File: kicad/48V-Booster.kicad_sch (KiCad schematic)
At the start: 14 parts, among them J9 48V out, U3 LM317_TO-220

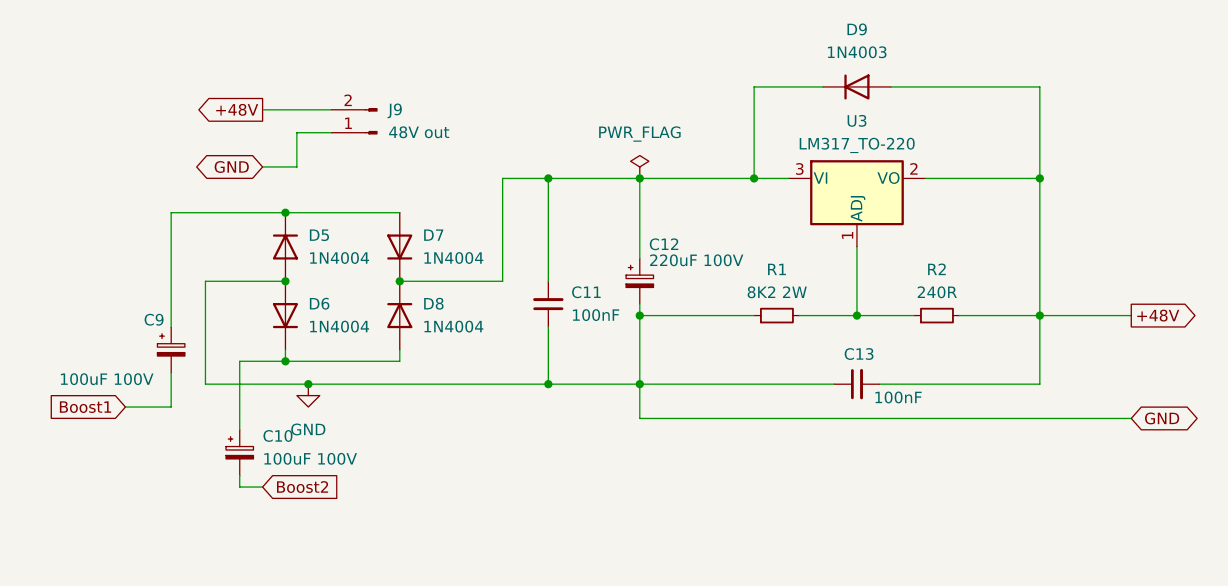
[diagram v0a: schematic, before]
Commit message: Board done - needs added text
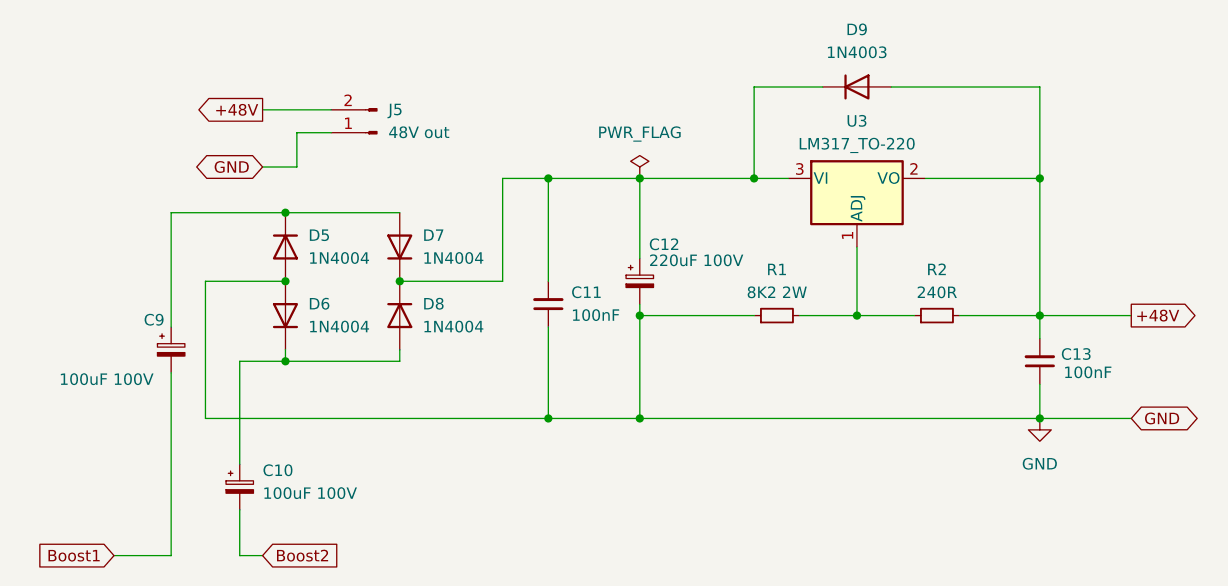
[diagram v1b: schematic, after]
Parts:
- renumbered J9 to J5
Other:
- moved on the sheet: C10

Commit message: Added scripts to generate non 48V version and a PCB and BOM for this
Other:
- company: Andrew Martin -> Andrew Martin, acramonics
- title: MHS PreAmp PSU -> Audio Power Supply
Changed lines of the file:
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@@
 	(paper "A4")
 	(title_block
-		(title "MHS PreAmp PSU")
-		(date "2025-09-24")
+		(title "Audio Power Supply")
+		(date "2026-07-09")
 		(rev "V1.0")
-		(company "Andrew Martin")
+		(company "Andrew Martin, acramonics")
+		(comment 1 "48V Booster")
 	)
 	(junction
